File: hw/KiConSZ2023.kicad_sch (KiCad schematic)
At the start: 2 parts, among them J4 Conn_02x03_Top_Bottom, J5 Conn_02x03_Top_Bottom

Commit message: updated sheets information
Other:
- company: (none) -> Qingdao IotPi Information Technology Ltd.,
- title: (none) -> KiCad 2023 Shen Zhen Badge
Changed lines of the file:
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@@
 (kicad_sch (version 20230121) (generator eeschema)
   (paper "A3")
+  (title_block
+    (title "KiCad 2023 Shen Zhen Badge")
+    (date "2023-09-04")
+    (rev "1")
+    (company "Qingdao IotPi Information Technology Ltd.,")
+    (comment 1 "Designed by Yang Hongbo")
+  )
   (wire (pts (xy 241.3 93.98) (xy 248.92 93.98))
     (stroke (width 0) (type default))

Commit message: changed Hardware design
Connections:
- no-connect marks 0 -> 23
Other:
- removed sheet LED Matrix
- removed sheet QMI8658A
- added sheet LED Row (LED_Row.kicad_sch)

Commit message: updated Designs
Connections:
- no-connect marks 23 -> 18
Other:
- sheet LED Row ports: added HighSide_Input_Row_10, HighSide_Input_Row_11, HighSide_Input_Row_12, HighSide_Input_Row_7, HighSide_Input_Row_8, HighSide_Input_Row_9; removed none
- sheet MCU ports: added HighSide_Row_1, HighSide_Row_10, HighSide_Row_11, HighSide_Row_12, HighSide_Row_2, HighSide_Row_3, HighSide_Row_4, HighSide_Row_5, HighSide_Row_6, HighSide_Row_7, HighSide_Row_8, HighSide_Row_9, LowSide_B_Col_1, LowSide_B_Col_2, LowSide_B_Col_3, LowSide_B_Col_4, LowSide_B_Col_5, LowSide_B_Col_6, LowSide_G_Col_1, LowSide_G_Col_2, LowSide_G_Col_3, LowSide_G_Col_4, LowSide_G_Col_5, LowSide_G_Col_6, LowSide_R_Col_1, LowSide_R_Col_2, LowSide_R_Col_3, LowSide_R_Col_4, LowSide_R_Col_5, LowSide_R_Col_6; removed HighSide_Input_Row_1, HighSide_Input_Row_2, HighSide_Input_Row_3, HighSide_Input_Row_4, HighSide_Input_Row_5, HighSide_Input_Row_6, HighSide_Input_Row_7, HighSide_Input_Row_8, LowSide_Input_B_Col_1, LowSide_Input_B_Col_2, LowSide_Input_B_Col_3, LowSide_Input_B_Col_4, LowSide_Input_B_Col_5, LowSide_Input_B_Col_6, LowSide_Input_G_Col_1, LowSide_Input_G_Col_2, LowSide_Input_G_Col_3, LowSide_Input_G_Col_4, LowSide_Input_G_Col_5, LowSide_Input_G_Col_6, LowSide_Input_R_Col_1, LowSide_Input_R_Col_2, LowSide_Input_R_Col_3, LowSide_Input_R_Col_4, LowSide_Input_R_Col_5, LowSide_Input_R_Col_6

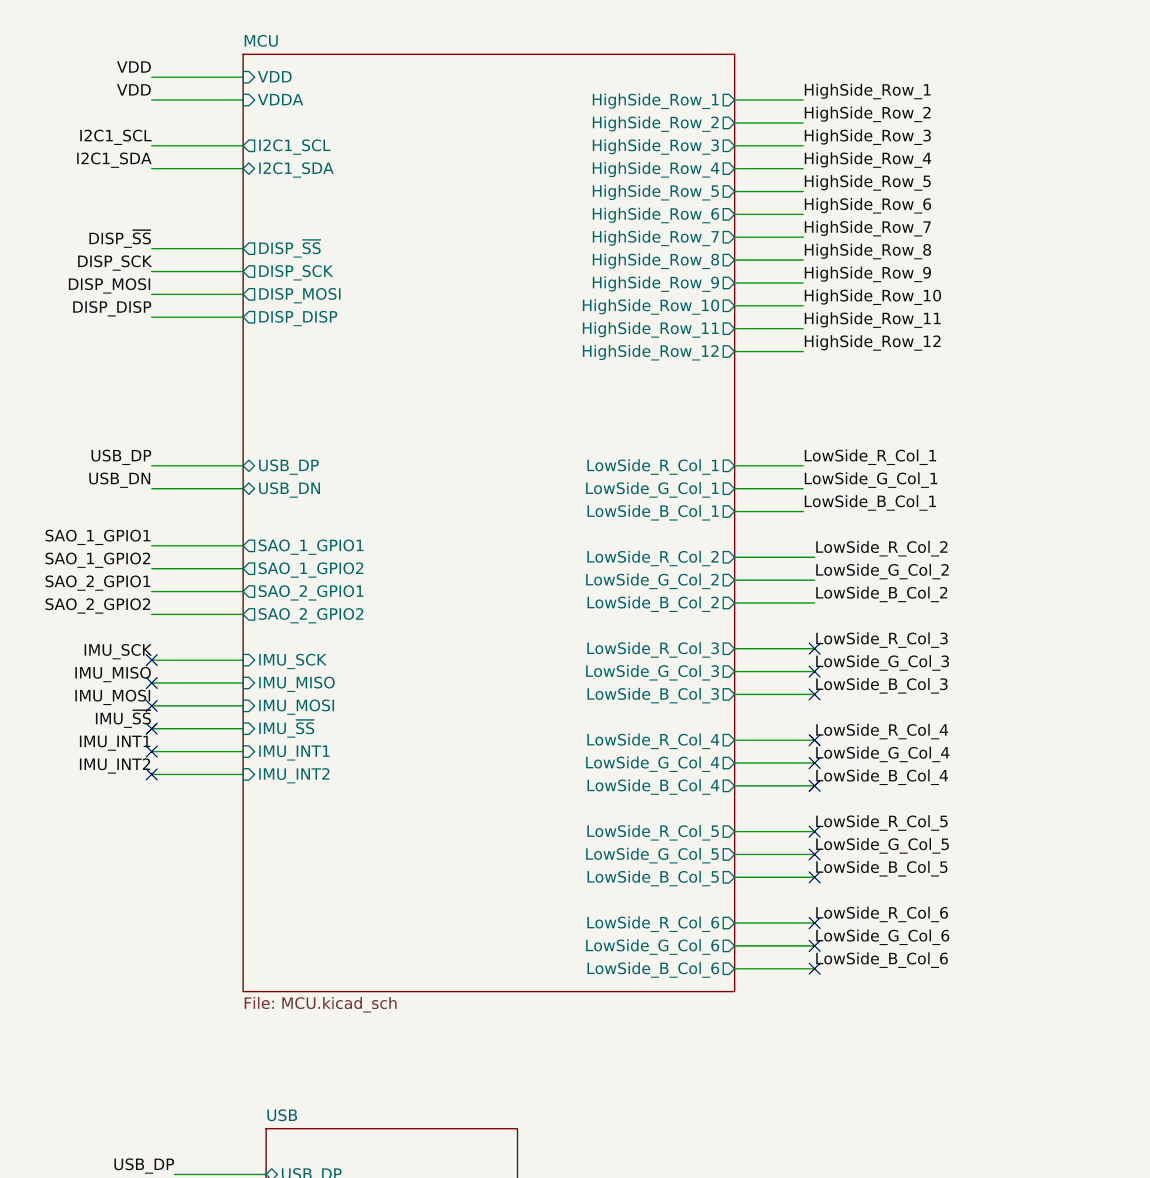
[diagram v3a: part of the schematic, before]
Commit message: routed HighSide MOS
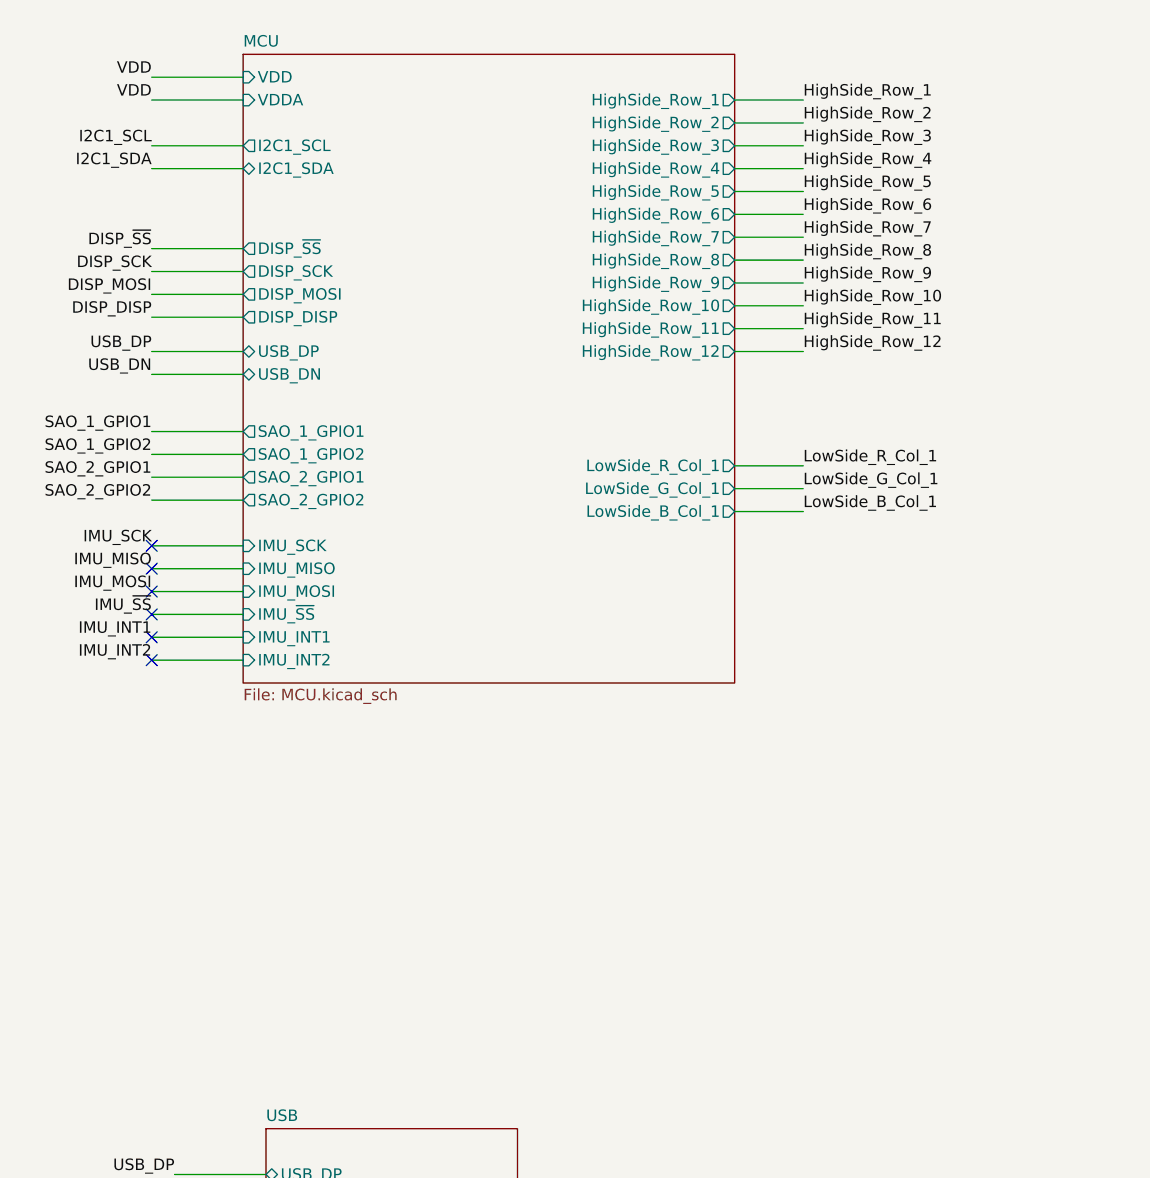
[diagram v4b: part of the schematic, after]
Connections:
- no-connect marks 18 -> 6
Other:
- sheet MCU ports: added none; removed LowSide_B_Col_2, LowSide_B_Col_3, LowSide_B_Col_4, LowSide_B_Col_5, LowSide_B_Col_6, LowSide_G_Col_2, LowSide_G_Col_3, LowSide_G_Col_4, LowSide_G_Col_5, LowSide_G_Col_6, LowSide_R_Col_2, LowSide_R_Col_3, LowSide_R_Col_4, LowSide_R_Col_5, LowSide_R_Col_6

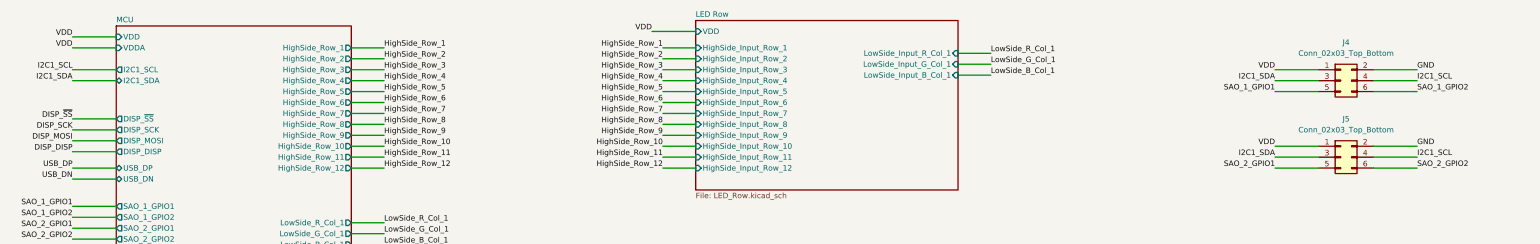
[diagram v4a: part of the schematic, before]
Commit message: routed SAO I2C
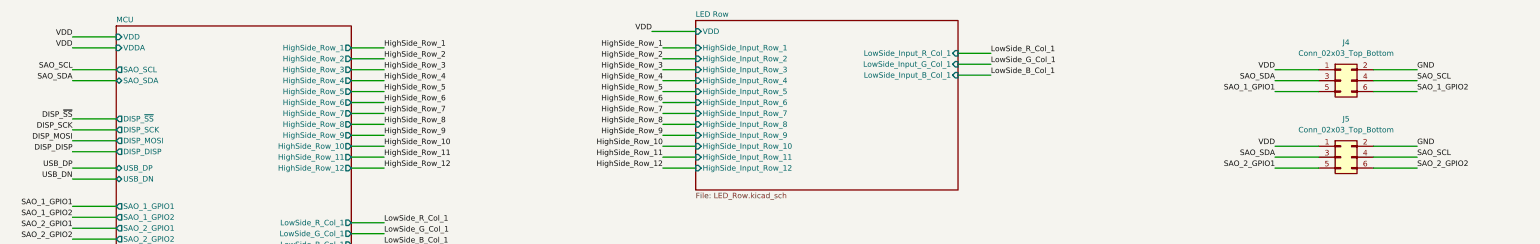
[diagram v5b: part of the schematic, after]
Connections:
- net I2C1_SCL renamed SAO_SCL
- net I2C1_SDA renamed SAO_SDA
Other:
- sheet MCU ports: added SAO_SCL, SAO_SDA; removed I2C1_SCL, I2C1_SDA
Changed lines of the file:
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@@
     (effects (font (size 1.27 1.27)) (justify right bottom))
   )
-  (label "I2C1_SDA" (at 312.42 60.96 180) (fields_autoplaced)
+  (label "SAO_SDA" (at 312.42 60.96 180) (fields_autoplaced)
     (effects (font (size 1.27 1.27)) (justify right bottom))
   )
@@
     (effects (font (size 1.27 1.27)) (justify left bottom))
   )
-  (label "I2C1_SDA" (at 312.42 78.74 180) (fields_autoplaced)
+  (label "SAO_SDA" (at 312.42 78.74 180) (fields_autoplaced)
     (effects (font (size 1.27 1.27)) (justify right bottom))
   )
@@
     (effects (font (size 1.27 1.27)) (justify right bottom))
   )
-  (label "I2C1_SCL" (at 345.44 60.96 0) (fields_autoplaced)
+  (label "SAO_SCL" (at 345.44 60.96 0) (fields_autoplaced)
     (effects (font (size 1.27 1.27)) (justify left bottom))
   )
@@
     (effects (font (size 1.27 1.27)) (justify right bottom))
   )
-  (label "I2C1_SCL" (at 33.02 58.42 180) (fields_autoplaced)
+  (label "SAO_SCL" (at 33.02 58.42 180) (fields_autoplaced)
     (effects (font (size 1.27 1.27)) (justify right bottom))
   )
@@
     (effects (font (size 1.27 1.27)) (justify left bottom))
   )
-  (label "I2C1_SCL" (at 345.44 78.74 0) (fields_autoplaced)
-    (effects (font (size 1.27 1.27)) (justify left bottom))
-  )
-  (label "I2C1_SDA" (at 33.02 60.96 180) (fields_autoplaced)
+  (label "SAO_SCL" (at 345.44 78.74 0) (fields_autoplaced)
+    (effects (font (size 1.27 1.27)) (justify left bottom))
+  )
+  (label "SAO_SDA" (at 33.02 60.96 180) (fields_autoplaced)
     (effects (font (size 1.27 1.27)) (justify right bottom))
   )
@@
       (effects (font (size 1.27 1.27)) (justify left))
     )
-    (pin "I2C1_SCL" output (at 43.18 58.42 180)
-      (effects (font (size 1.27 1.27)) (justify left))
-    )
-    (pin "I2C1_SDA" bidirectional (at 43.18 60.96 180)
-      (effects (font (size 1.27 1.27)) (justify left))
-    )
     (pin "DISP_~{SS}" output (at 43.18 69.85 180)
       (effects (font (size 1.27 1.27)) (justify left))
@@
       (effects (font (size 1.27 1.27)) (justify right))
     )
-    (instances
+    (pin "SAO_SCL" output (at 43.18 58.42 180)
+      (effects (font (size 1.27 1.27)) (justify left))
+    )
+    (pin "SAO_SDA" bidirectional (at 43.18 60.96 180)
+      (effects (font (size 1.27 1.27)) (justify left))
+    )
+    (instances
